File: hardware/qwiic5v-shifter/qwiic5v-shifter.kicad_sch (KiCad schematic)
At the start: 15 parts, among them J1 QWIIC Connector, J2 QWIIC Connector, Q1 2N7002, Q2 2N7002, U1 LTC3203BEDD-PBF

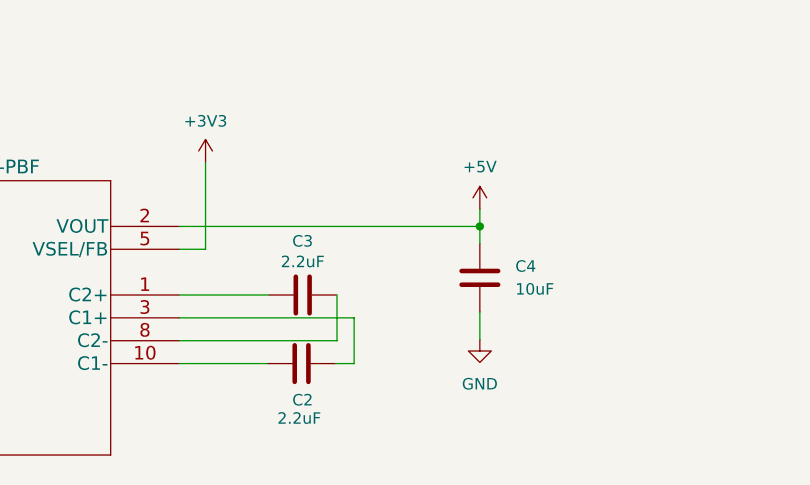
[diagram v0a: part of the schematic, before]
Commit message: Forgot to mark the max current
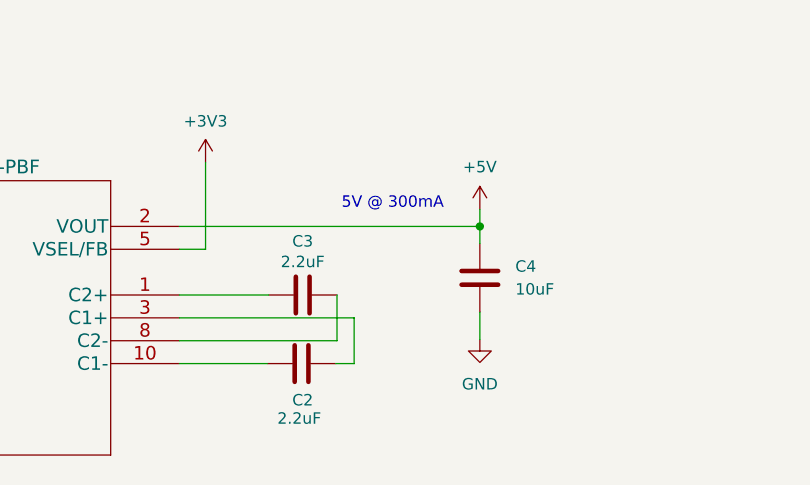
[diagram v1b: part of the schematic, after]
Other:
- note added: "5V @ 300mA"
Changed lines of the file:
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@@
     (stroke (width 0) (type default) (color 0 0 0 0))
+  )
+  (text "5V @ 300mA" (at 188.976 75.946 0)
+    (effects (font (size 1.27 1.27)) (justify left bottom))
   )
   (global_label "SCL5V" (shape bidirectional) (at 127.127 135.763 0) (fields_autoplaced)

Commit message: Added title block info, added PDFs
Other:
- company: (none) -> Gavin Hurlbut
- title: (none) -> QWIIC 5V Shifter
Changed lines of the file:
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@@
 (kicad_sch (version 20211123) (generator eeschema)
   (paper "A4")
+  (title_block
+    (title "QWIIC 5V Shifter")
+    (date "2023-01-31")
+    (rev "1.0")
+    (company "Gavin Hurlbut")
+  )
   (junction (at 255.27 115.697) (diameter 0) (color 0 0 0 0)
   )

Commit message: Move the gates of the level translators to the lowside signal
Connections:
- net +3V3: no longer Q1.1 (G), Q2.1 (G)
- net SCL3V: now also Q2.1 (G)
- net SDA3V: now also Q1.1 (G)
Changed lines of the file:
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@@
   (title_block
     (title "QWIIC 5V Shifter")
-    (date "2023-01-31")
-    (rev "1.0")
+    (date "2023-02-05")
+    (rev "2.0")
     (company "Gavin Hurlbut")
   )
@@
   (junction (at 47.244 108.839) (diameter 0) (color 0 0 0 0)
   )
+  (junction (at 108.966 164.973) (diameter 0) (color 0 0 0 0)
+  )
+  (junction (at 109.982 135.763) (diameter 0) (color 0 0 0 0)
+  )
   (wire (pts (xy 46.482 108.839) (xy 47.244 108.839))
     (stroke (width 0) (type default) (color 0 0 0 0))
@@
     (stroke (width 0) (type default) (color 0 0 0 0))
   )
+  (wire (pts (xy 108.966 164.973) (xy 110.998 164.973))
+    (stroke (width 0) (type default) (color 0 0 0 0))
+  )
+  (wire (pts (xy 109.982 125.349) (xy 109.982 135.763))
+    (stroke (width 0) (type default) (color 0 0 0 0))
+  )
   (wire (pts (xy 116.078 154.559) (xy 116.078 157.353))
     (stroke (width 0) (type default) (color 0 0 0 0))
@@
     (stroke (width 0) (type default) (color 0 0 0 0))
   )
-  (wire (pts (xy 107.823 135.763) (xy 111.506 135.763))
+  (wire (pts (xy 107.823 135.763) (xy 109.982 135.763))
     (stroke (width 0) (type default) (color 0 0 0 0))
   )
@@
     (stroke (width 0) (type default) (color 0 0 0 0))
   )
+  (wire (pts (xy 109.982 135.763) (xy 111.506 135.763))
+    (stroke (width 0) (type default) (color 0 0 0 0))
+  )
+  (wire (pts (xy 116.586 125.349) (xy 109.982 125.349))
+    (stroke (width 0) (type default) (color 0 0 0 0))
+  )
   (wire (pts (xy 58.42 82.169) (xy 58.42 83.693))
     (stroke (width 0) (type default) (color 0 0 0 0))
@@
     (stroke (width 0) (type default) (color 0 0 0 0))
   )
+  (wire (pts (xy 108.966 154.559) (xy 108.966 164.973))
+    (stroke (width 0) (type default) (color 0 0 0 0))
+  )
+  (wire (pts (xy 116.078 154.559) (xy 108.966 154.559))
+    (stroke (width 0) (type default) (color 0 0 0 0))
+  )
   (wire (pts (xy 256.032 113.157) (xy 247.904 113.157))
     (stroke (width 0) (type default) (color 0 0 0 0))
@@
     (stroke (width 0) (type default) (color 0 0 0 0))
   )
-  (wire (pts (xy 107.061 164.973) (xy 110.998 164.973))
+  (wire (pts (xy 107.061 164.973) (xy 108.966 164.973))
     (stroke (width 0) (type default) (color 0 0 0 0))
   )
@@
     )
     (property "Datasheet" "" (id 3) (at 51.562 117.475 0)
-      (effects (font (size 1.27 1.27)) hide)
-    )
-    (pin "1")
-  )
-  (symbol (lib_id "power:+3V3") (at 116.078 154.559 0) (unit 1)
-    (in_bom yes) (on_board yes) (fields_autoplaced)
-    (property "Reference" "#PWR07" (id 0) (at 116.078 158.369 0)
-      (effects (font (size 1.27 1.27)) hide)
-    )
-    (property "Value" "+3V3" (id 1) (at 116.078 149.86 0))
-    (property "Footprint" "" (id 2) (at 116.078 154.559 0)
-      (effects (font (size 1.27 1.27)) hide)
-    )
-    (property "Datasheet" "" (id 3) (at 116.078 154.559 0)
       (effects (font (size 1.27 1.27)) hide)
     )
@@
     )
     (property "Datasheet" "" (id 3) (at 117.475 100.838 0)
-      (effects (font (size 1.27 1.27)) hide)
-    )
-    (pin "1")
-  )
-  (symbol (lib_id "power:+3V3") (at 116.586 125.349 0) (unit 1)
-    (in_bom yes) (on_board yes) (fields_autoplaced)
-    (property "Reference" "#PWR08" (id 0) (at 116.586 129.159 0)
-      (effects (font (size 1.27 1.27)) hide)
-    )
-    (property "Value" "+3V3" (id 1) (at 116.586 120.65 0))
-    (property "Footprint" "" (id 2) (at 116.586 125.349 0)
-      (effects (font (size 1.27 1.27)) hide)
-    )
-    (property "Datasheet" "" (id 3) (at 116.586 125.349 0)
       (effects (font (size 1.27 1.27)) hide)
     )
@@
       (reference "#PWR06") (unit 1) (value "GND") (footprint "")
     )
-    (path "/2f9961f0-e1e8-4feb-88f1-14085a2ecf32"
-      (reference "#PWR07") (unit 1) (value "+3V3") (footprint "")
-    )
-    (path "/8ff3c27f-3c87-44c8-bb23-0db6364f78d8"
-      (reference "#PWR08") (unit 1) (value "+3V3") (footprint "")
-    )
     (path "/8bf620b4-91c0-4973-99d0-55adfc012245"
